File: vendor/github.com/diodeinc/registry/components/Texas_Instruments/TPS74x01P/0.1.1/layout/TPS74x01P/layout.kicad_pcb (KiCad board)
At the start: 2 copper layers, 6 parts, among them IC1 TPS74501PCQWDRVRQ1

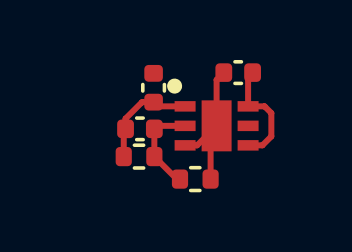
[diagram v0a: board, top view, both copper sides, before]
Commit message: feat(Feign): switch to TPS74x01P LDO and TPS2553DRV load switch
Replace reference/TPS745x with components/Texas_Instruments/TPS74x01P
for the 3V3 ULDO. Add components/Texas_Instruments/TPS2553DRV as the
finalized 5V VCC_OUT load switch (auto-retry, 500 mA). Bump pinned
versions of STM32G0B1KxUxN, TPD4E05U06QDQARQ1, and UsbCSink16P to
their latest patches as resolved by pcb build.
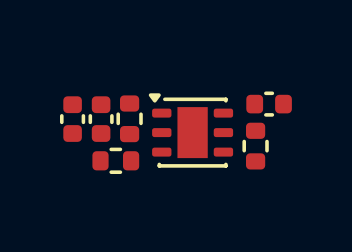
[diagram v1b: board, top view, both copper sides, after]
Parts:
- removed IC1: TPS74501PCQWDRVRQ1, TPS74501PCQWDRVRQ1:TPS74501PCQWDRVRQ1
- added R3: ERJ-2RKF2553X, kicad_libraries_kicad-footprints_Resistor_SMD@9.0.3:R_0402_1005Metric, F.Cu at (145.6, 104.9)
- added U1: TPS74501PDRVR, diodeinc_registry_components_Texas_Instruments_TPS74x01P:TPS74x01P, F.Cu at (147.7, 105.3)
- C1: footprint C_0402_1005Metric:C_0402_1005Metric -> kicad_libraries_kicad-footprints_Capacitor_SMD@9.0.3:C_0402_1005Metric
- C2, C3: value GRM155Z71A225KE44D -> GRM155Z71A105KE01D; footprint C_0402_1005Metric:C_0402_1005Metric -> kicad_libraries_kicad-footprints_Capacitor_SMD@9.0.3:C_0402_1005Metric
- R1: value ERJ-2RKF5602X -> ERJ-2RKF1003X; footprint R_0402_1005Metric:R_0402_1005Metric -> kicad_libraries_kicad-footprints_Resistor_SMD@9.0.3:R_0402_1005Metric
- R2: value ERJ-2RKF1273X -> ERJ-2RKF5102X; footprint R_0402_1005Metric:R_0402_1005Metric -> kicad_libraries_kicad-footprints_Resistor_SMD@9.0.3:R_0402_1005Metric
- moved C3 2.90 mm to (143.7, 104.9), turned to -90 degrees
- moved R1 2.29 mm to (149.8, 105.8), turned to -90 degrees
- moved C2 1.47 mm to (150.2, 104.4), turned to 0 degrees
- moved C1 1.34 mm to (144.7, 104.9), turned to -90 degrees
- moved R2 0.79 mm to (145.1, 106.3)
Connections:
- C1 pad 1: _FB -> VOUT
- C1 pad 2: VOUT -> _FB
- R1 pad 1: _FB -> VIN
- R1 pad 2: GND -> EN
- R2 pad 1: VOUT -> _FB
- R2 pad 2: _FB -> GND
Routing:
- net GND: track 5.05 -> 0.00 mm
- net VIN: track 3.73 -> 0.00 mm
- net VOUT: track 3.56 -> 0.00 mm
- net _FB: track 3.16 -> 0.00 mm
